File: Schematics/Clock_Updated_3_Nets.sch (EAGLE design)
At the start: 53 parts, among them U1 ATMEGA328P

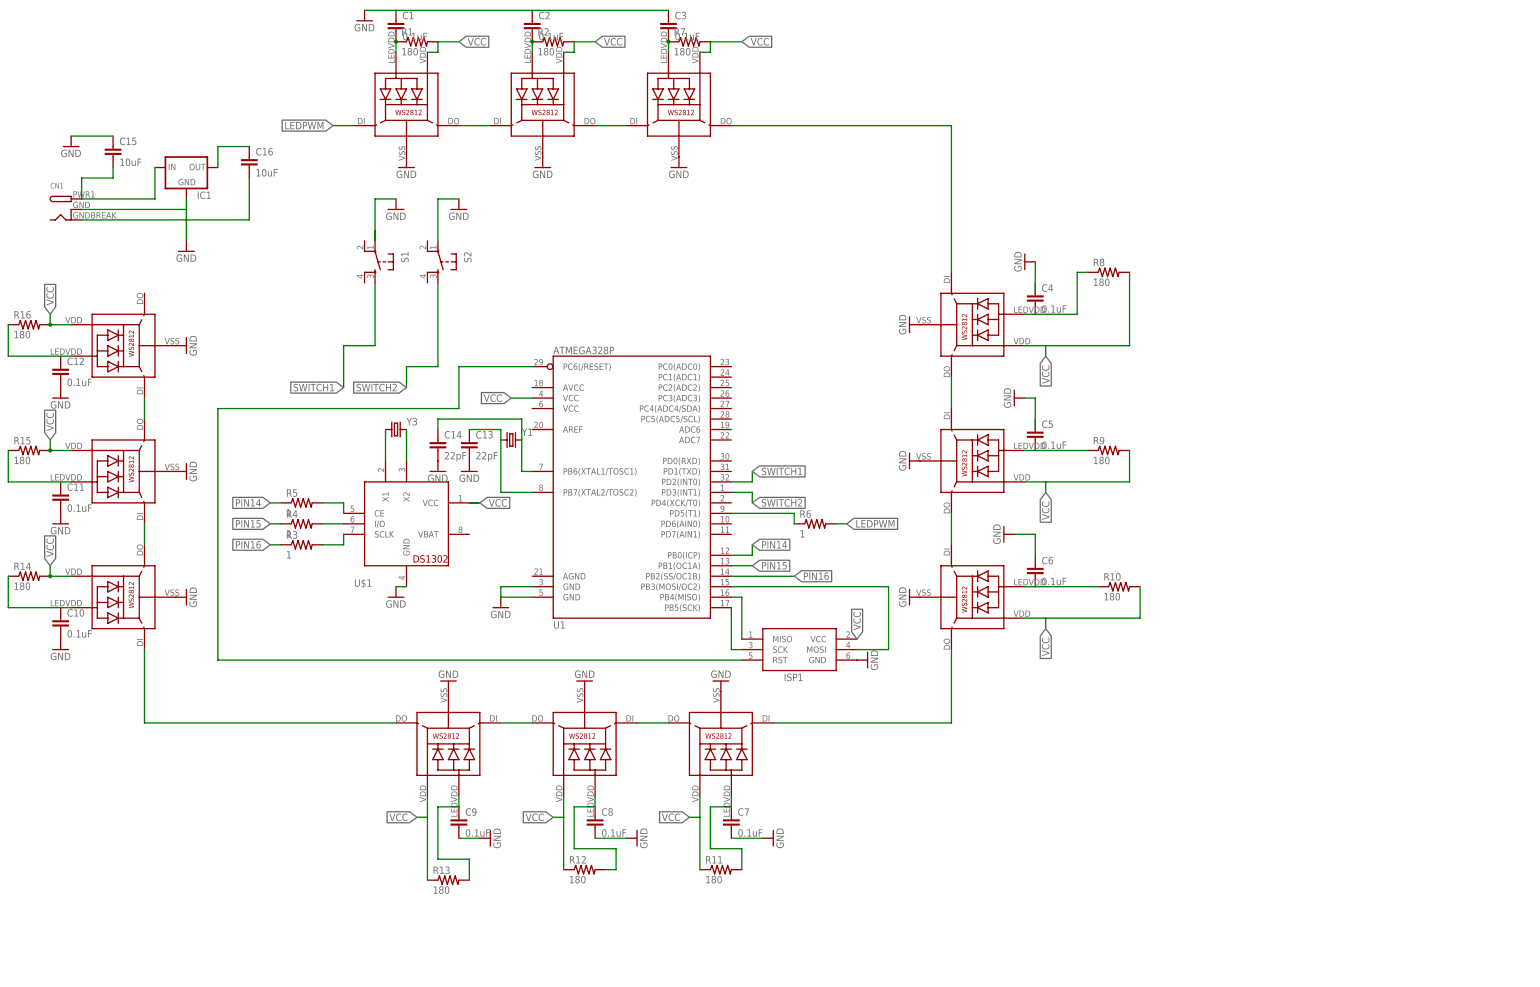
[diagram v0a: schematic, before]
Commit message: found out vdd and ledvdd were switched
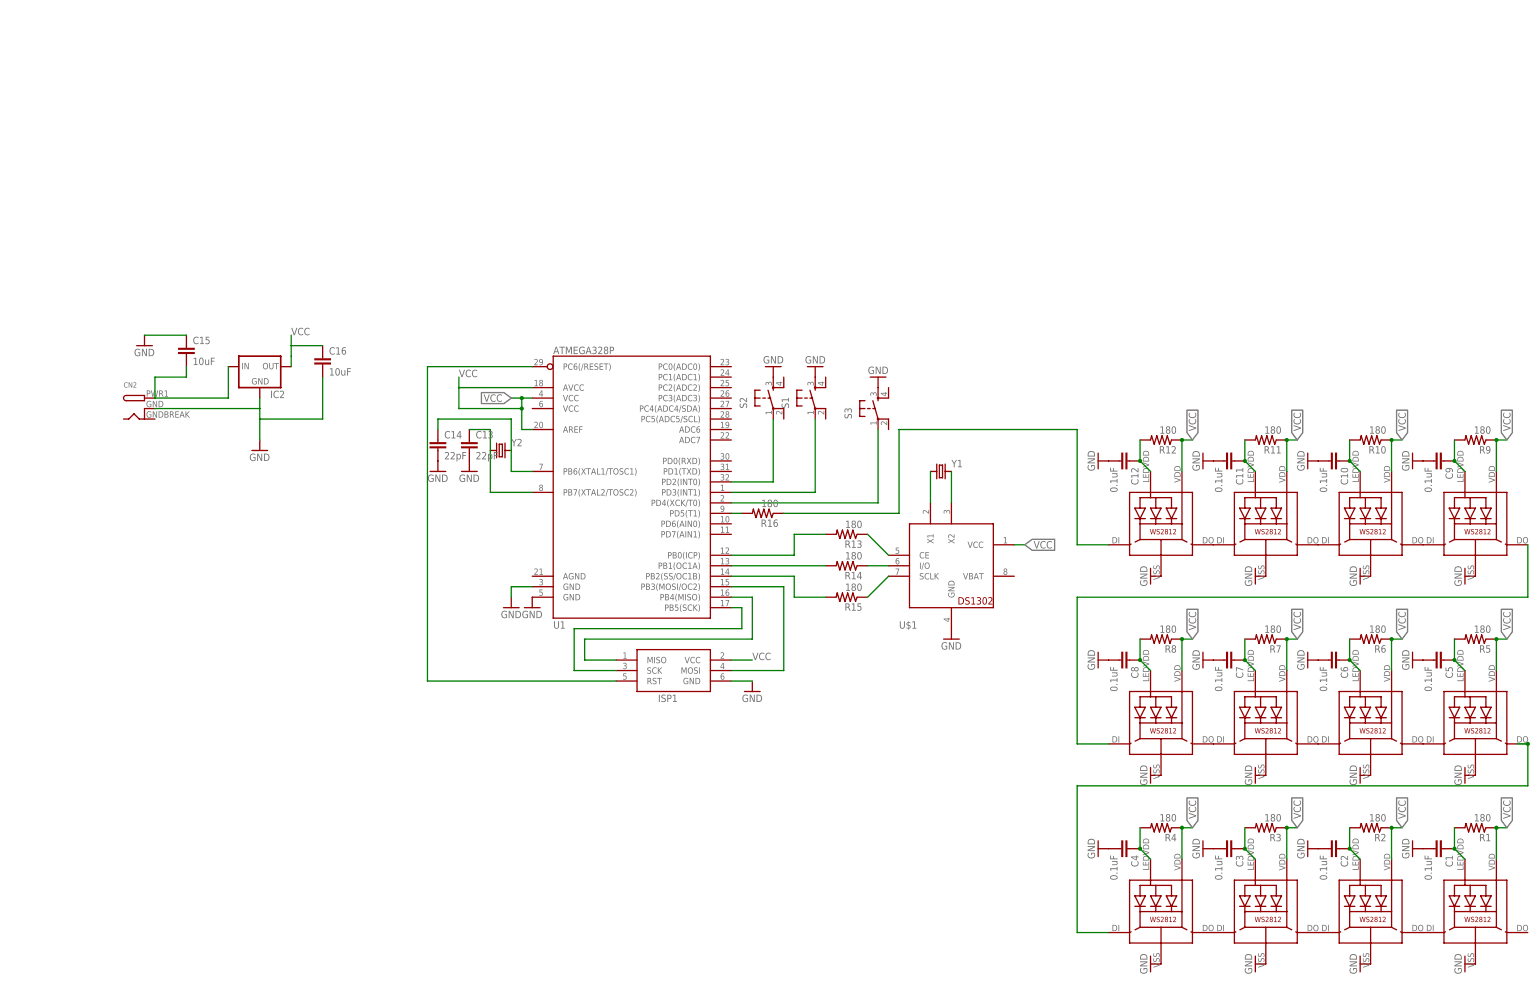
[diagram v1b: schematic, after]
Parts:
- removed CN1: (no value), adafruit:DCBARRELSMT
- removed IC1: (no value), SparkFun-PowerIC:V_REG_78XX-TO-220
- removed Y3: (no value), SparkFun-FreqCtrl:CRYSTAL32-SMD
- added CN2: (no value), adafruit:DCBARRELSMT
- added IC2: (no value), SparkFun-PowerIC:V_REG_78XX-TO-220
- added S3: (no value), SparkFun-Electromechanical:TAC_SWITCHPTH
- added Y2: (no value), SparkFun-FreqCtrl:CRYSTALSMD
- R3, R4, R5, R6: value 1 -> 180; device SparkFun-Resistors:1OHM1/10W1%(0603) -> SparkFun-Resistors:180OHM1/10W1%(0603)
- Y1: device SparkFun-FreqCtrl:CRYSTALSMD -> SparkFun-FreqCtrl:CRYSTALTC38H
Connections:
- removed net LEDPWM: LED1.DI, R6.2
- removed net N$1: R6.1, U1.PD5(T1)
- removed net N$2: C4.2, LED5.LEDVDD, R8.1
- removed net N$3: C5.2, LED6.LEDVDD, R9.1
- removed net N$36 (its old number): C15.2, CN1.PWR, IC1.IN
- removed net PIN14: R5.1, U1.PB0(ICP)
- removed net PIN15: R4.1, U1.PB1(OC1A)
- removed net PIN16: R3.1, U1.PB2(SS/OC1B)
- removed net SWITCH1: S1.3, U1.PD2(INT0)
- removed net SWITCH2: S2.3, U1.PD3(INT1)
- new net N$40: LED2.DI, LED3.DO
- new net N$41: LED6.DI, LED7.DO
- new net N$42: LED10.DI, LED11.DO
- new net N$43: LED12.DI, R16.1
- new net N$44: C14.1, Y2.2
- new net N$45: C15.2, CN2.PWR, IC2.IN
- net GND: now also C1.2, C2.2, C3.2, C4.2, C5.2, C6.2, CN2.GNDBREAK, IC2.GND, S1.3, S2.3, S3.3; no longer C1.1, C3.1, C6.1, CN1.GND, CN1.GNDBREAK, IC1.GND, S1.1, S2.1
- net N$10: now also C3.1, LED3.LEDVDD, R3.2; no longer R4.2, U$1.I/O
- net N$11: now also C4.1, LED4.LEDVDD, R4.2; no longer R5.2, U$1.CE
- net N$12: now also LED3.DI, LED4.DO; no longer LED11.DO, LED4.DI
- net N$13: now also C5.1, LED5.LEDVDD, R5.2; no longer LED6.VDD, R9.2
- net N$14: now also C6.1, LED6.LEDVDD, R6.2; no longer LED12.DI, LED8.DO
- net N$15: now also LED5.DI, LED6.DO; no longer C7.1, LED9.LEDVDD, R11.2
- net N$16: now also C7.1, LED7.LEDVDD, R7.2; no longer LED6.DO, LED7.DI
- net N$17: now also C8.1, LED8.LEDVDD, R8.2; no longer LED3.DO, LED5.DI
- net N$18: now also LED7.DI, LED8.DO; no longer LED5.DO, LED6.DI
- net N$19: now also C9.1, LED9.LEDVDD, R9.2; no longer LED1.DO, LED2.DI
- net N$20: now also C10.1, LED10.LEDVDD, R10.2; no longer LED2.DO, LED3.DI
- net N$21: now also LED10.DO, LED9.DI; no longer C8.1, LED10.LEDVDD
- net N$22: now also C11.1, LED11.LEDVDD, R11.2; no longer LED4.DO, LED8.DI
- net N$23: now also C12.1, LED12.LEDVDD, R12.2; no longer C9.1, LED11.LEDVDD, R13.2
- net N$24: now also LED11.DI, LED12.DO; no longer LED12.LEDVDD, R16.1
- net N$25: now also LED4.DI, LED5.DO; no longer LED7.DO, LED9.DI
- net N$26: now also LED8.DI, LED9.DO; no longer R12.2
- net N$27: now also R13.1, U$1.CE; no longer LED4.LEDVDD, R14.1
- net N$28: now also R14.1, U$1.I/O; no longer ISP1.MOSI, U1.PB3(MOSI/OC2)
- net N$29: now also U$1.SCLK; no longer LED8.LEDVDD
- net N$30: now also S1.1, U1.PD3(INT1); no longer C1.2, LED1.LEDVDD, R1.1
- net N$31: now also R14.2, U1.PB1(OC1A); no longer C2.2, LED2.LEDVDD, R2.1
- net N$32: now also R13.2, U1.PB0(ICP); no longer C3.2, LED3.LEDVDD, R7.1
- net N$33: now also R15.2, U1.PB2(SS/OC1B); no longer ISP1.MISO, U1.PB4(MISO)
- net N$37: now also S3.1, U1.PD4(XCK/T0); no longer C16.1, IC1.OUT
- net N$38: now also Y2.1; no longer Y1.1
- net N$39: now also R16.2, U1.PD5(T1); no longer C14.1, U1.PB6(XTAL1/TOSC1), Y1.2
- net N$4: now also S2.1, U1.PD2(INT0); no longer C6.2, LED7.LEDVDD, R10.1
- net N$5: now also U$1.X2, Y1.2; no longer LED10.DI, LED9.DO
- net N$6: now also U$1.X1, Y1.1; no longer LED10.DO, LED11.DI
- net N$7: now also C1.1, LED1.LEDVDD, R1.2; no longer U$1.X2, Y3.2
- net N$8: now also C2.1, LED2.LEDVDD, R2.2; no longer U$1.X1, Y3.1
- net N$9: now also LED1.DI, LED2.DO; no longer R3.2, U$1.SCLK
- net VCC: now also C16.1, IC2.OUT, ISP1.MISO, ISP1.MOSI, ISP1.VCC, LED6.VDD, R1.1, R10.1, R2.1, R3.1, R4.1, R5.1, R6.1, R7.1, R8.1, R9.1, U1.AREF, U1.PB3(MOSI/OC2), U1.PB4(MISO); no longer R10.2, R13.1, R14.2, R15.2, R16.2, R8.2
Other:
- moved on the sheet: C1, C10, C11, C12, C15, C16, C2, C3, C4, C5, C6, C7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
